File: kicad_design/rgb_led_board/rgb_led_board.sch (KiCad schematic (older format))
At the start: 6 parts, among them P1 CONN_2, P2 CONN_2, U1 RGB_MULTILED

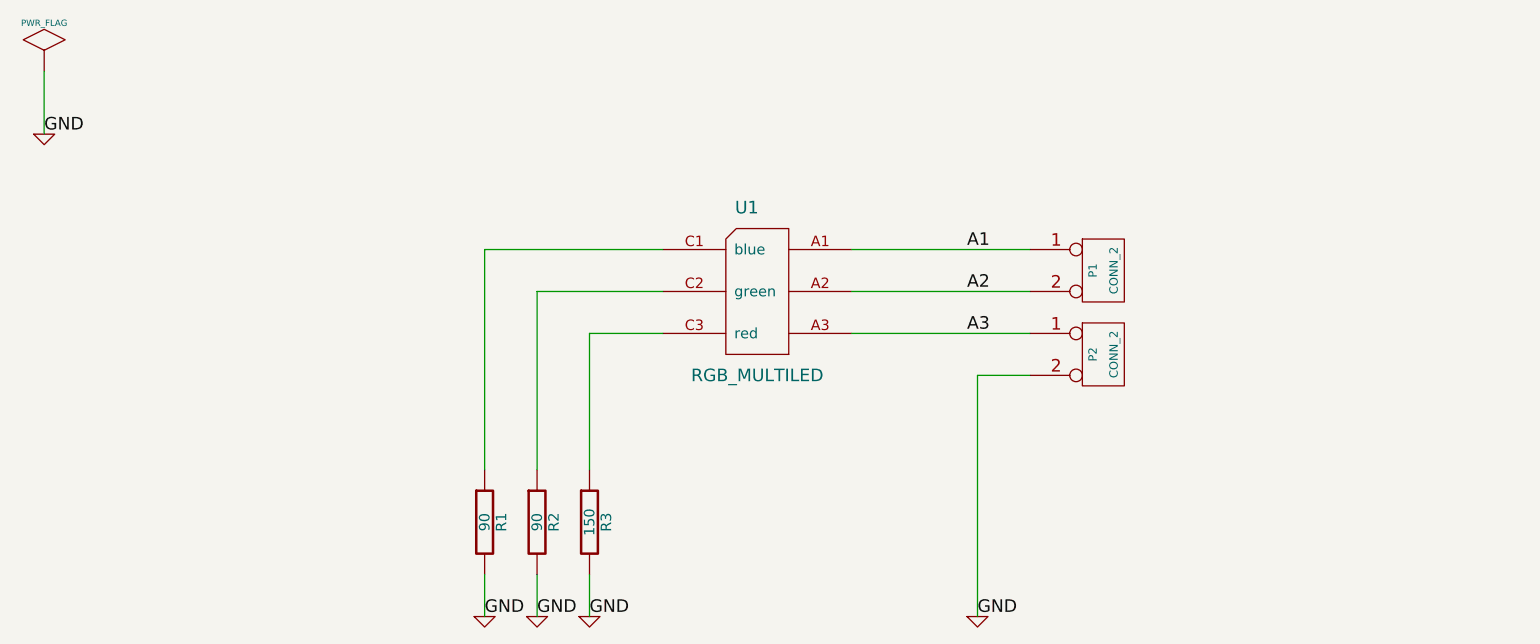
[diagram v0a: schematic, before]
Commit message: Changes to the sensor and LED boards to replace the terminal blocks with surface mount components.
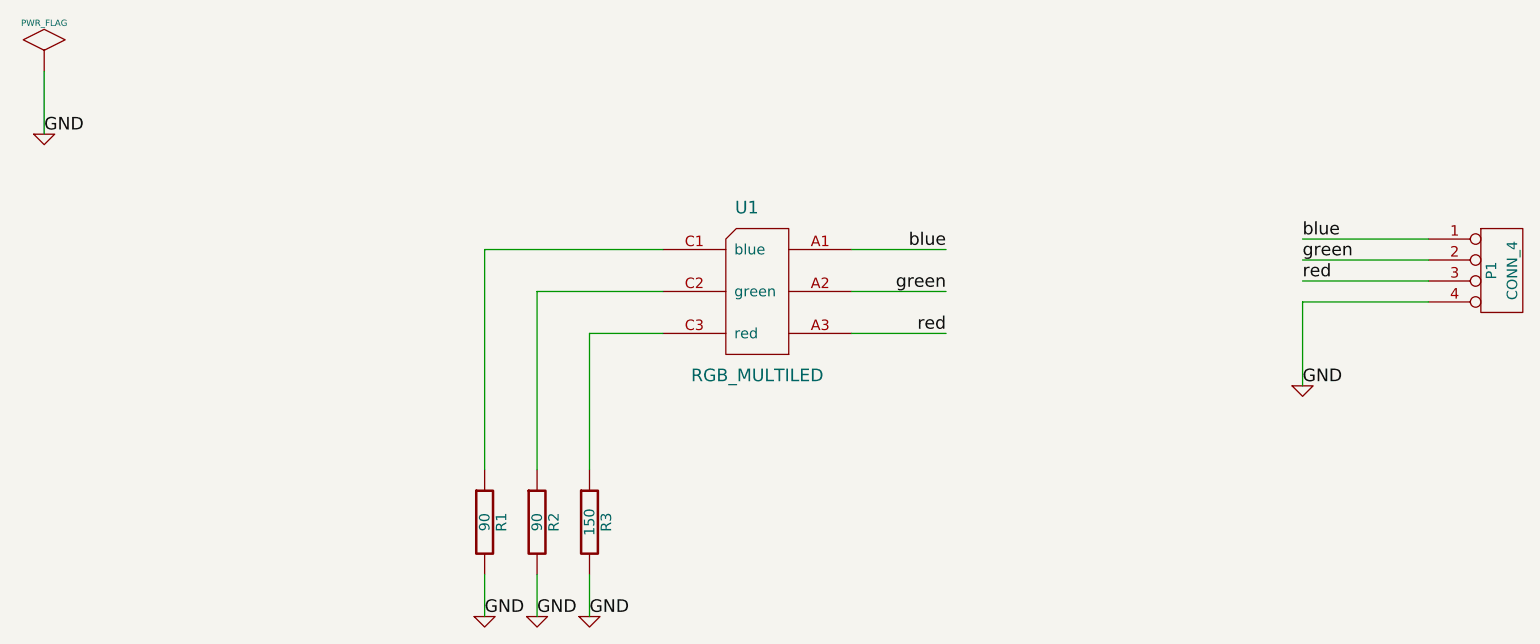
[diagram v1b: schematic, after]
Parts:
- removed P1, P2: CONN_2, symbol CONN_2
- added P1: CONN_4, symbol CONN_4
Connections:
- net GND: now also P1.4 (P4)
- net A1 renamed blue
- net blue: now also P1.1 (P1)
- net A2 renamed green
- net green: now also P1.2 (P2)
- net A3 renamed red
- net red: now also P1.3 (P3)
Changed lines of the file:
@@
-EESchema Schematic File Version 2  date Tue 03 Jan 2012 12:05:37 PM PST
+EESchema Schematic File Version 2  date Thu 09 Feb 2012 04:13:39 PM PST
 LIBS:power
 LIBS:device
@@
 LIBS:valves
 LIBS:rgb_multiled
-EELAYER 43  0
+LIBS:rgb_led_board-cache
+EELAYER 25  0
 EELAYER END
 $Descr A4 11700 8267
@@
 Sheet 1 1
 Title ""
-Date "3 jan 2012"
+Date "10 feb 2012"
 Rev ""
 Comp ""
@@
 Comment4 ""
 $EndDescr
+Text Label 7000 3150 2    60   ~ 0
+red
+Text Label 7000 2950 2    60   ~ 0
+green
+Wire Wire Line
+	6550 3150 7000 3150
+Wire Wire Line
+	6550 2750 7000 2750
+Wire Wire Line
+	9300 3000 8700 3000
+Wire Wire Line
+	9300 2800 8700 2800
 Wire Wire Line
 	4800 3800 4800 2750
@@
 	5300 4300 5300 4500
 Wire Wire Line
-	7400 3350 7150 3350
-Wire Wire Line
-	6550 2950 7400 2950
-Wire Wire Line
 	2700 1900 2700 2200
 Wire Wire Line
-	6550 2750 7400 2750
-Wire Wire Line
-	6550 3150 7400 3150
-Wire Wire Line
 	5650 3150 5300 3150
 Wire Wire Line
@@
 	5050 2950 5050 3800
 Wire Wire Line
-	7150 3350 7150 4500
+	9300 2700 8700 2700
+Wire Wire Line
+	9300 2900 8700 2900
+Wire Wire Line
+	8700 3000 8700 3400
+Wire Wire Line
+	6550 2950 7000 2950
+Text Label 7000 2750 2    60   ~ 0
+blue
+Text Label 8700 2900 0    60   ~ 0
+red
+Text Label 8700 2800 0    60   ~ 0
+green
+Text Label 8700 2700 0    60   ~ 0
+blue
+$Comp
+L CONN_4 P1
+U 1 1 4F345F7F
+P 9650 2850
+F 0 "P1" V 9600 2850 50  0000 C CNN
+F 1 "CONN_4" V 9700 2850 50  0000 C CNN
+	1    9650 2850
+	1    0    0    -1
+$EndComp
 Text Label 4800 4500 0    60   ~ 0
 GND
@@
 Text Label 5300 4500 0    60   ~ 0
 GND
-Text Label 7150 4500 0    60   ~ 0
-GND
-Text Label 7100 3150 0    60   ~ 0
-A3
-Text Label 7100 2950 0    60   ~ 0
-A2
-Text Label 7100 2750 0    60   ~ 0
-A1
+Text Label 8700 3400 0    60   ~ 0
+GND
 Text Label 2700 2200 0    60   ~ 0
 GND
@@
 L GND #PWR04
 U 1 1 4F035C8B
-P 7150 4500
-F 0 "#PWR04" H 7150 4500 30  0001 C CNN
-F 1 "GND" H 7150 4430 30  0001 C CNN
-	1    7150 4500
+P 8700 3400
+F 0 "#PWR04" H 8700 3400 30  0001 C CNN
+F 1 "GND" H 8700 3330 30  0001 C CNN
+	1    8700 3400
 	1    0    0    -1
 $EndComp
@@
 	1    0    0    -1
 $EndComp
-$Comp
-L CONN_2 P2
-U 1 1 4F035C74
-P 7750 3250
-F 0 "P2" V 7700 3250 40  0000 C CNN
-F 1 "CONN_2" V 7800 3250 40  0000 C CNN
-	1    7750 3250
-	1    0    0    -1
-$EndComp
-$Comp
-L CONN_2 P1
-U 1 1 4F035C71
-P 7750 2850
-F 0 "P1" V 7700 2850 40  0000 C CNN
-F 1 "CONN_2" V 7800 2850 40  0000 C CNN
-	1    7750 2850
-	1    0    0    -1
-$EndComp
